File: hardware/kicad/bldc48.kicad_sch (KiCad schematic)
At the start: 0 parts

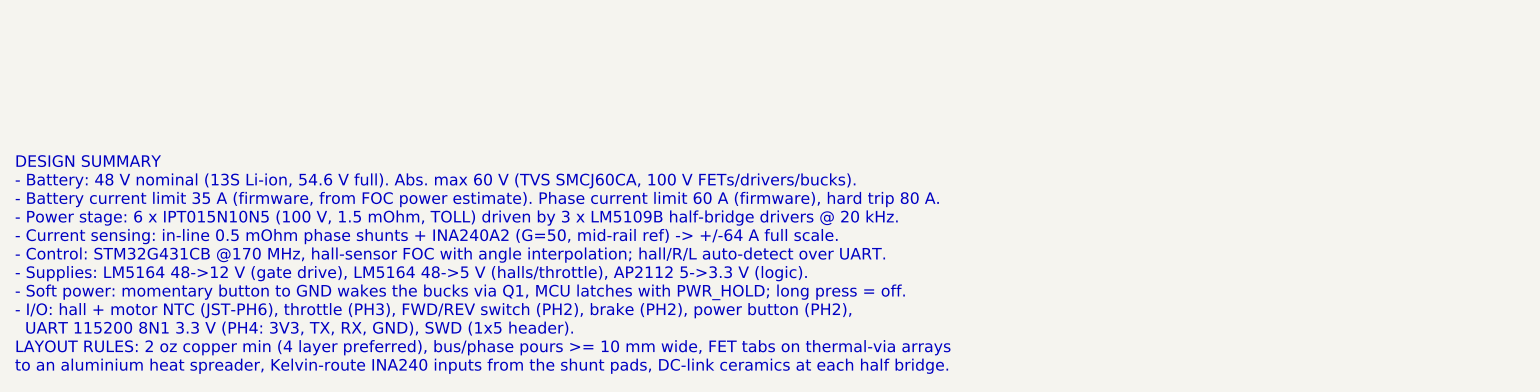
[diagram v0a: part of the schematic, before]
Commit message: Rev B: fix power terminals and design-review findings
Layout (hand-placed power stage):
- BAT+/BAT- and MOTOR A/B/C are now M5 plated bolt terminals at the board
  edges (battery 36 mm apart on the left edge, motors under their shunts),
  replacing 5x10 mm SMD solder pads that sat 7.5 mm apart
- per phase: driver | high FET over low FET (drain tabs up, compact switch
  node) | Kelvin shunt + INA240; DC-link ceramics at the low-side sources
- FET NTC moved next to the middle low-side FET
- rule area keeps tracks off the inner planes under the power stage
- pours sized from real TOLL pad outlines; solid plane connections
- hand route for the one connection Freerouting leaves open; routing
  session saved so the board rebuilds without the autorouter
- KiCad DRC: 0 violations, 0 unconnected, footprints match library

Schematic / firmware:
- INA240A2 -> INA240A1: the 80 A hard trip was above the old +/-66 A ADC
  full scale and could never fire; compile-time assert + sim test added
- 4-terminal Kelvin shunts (BVR 4026) feed the INA240 sense inputs
- gate resistors 10R -> 4R7, bulk caps 6 -> 8

Co-Authored-By: Claude Opus 5.5 <noreply@anthropic.com>
Claude-Session: https://claude.ai/code/session_01KE5bAkgcicsoh5erUtagKE
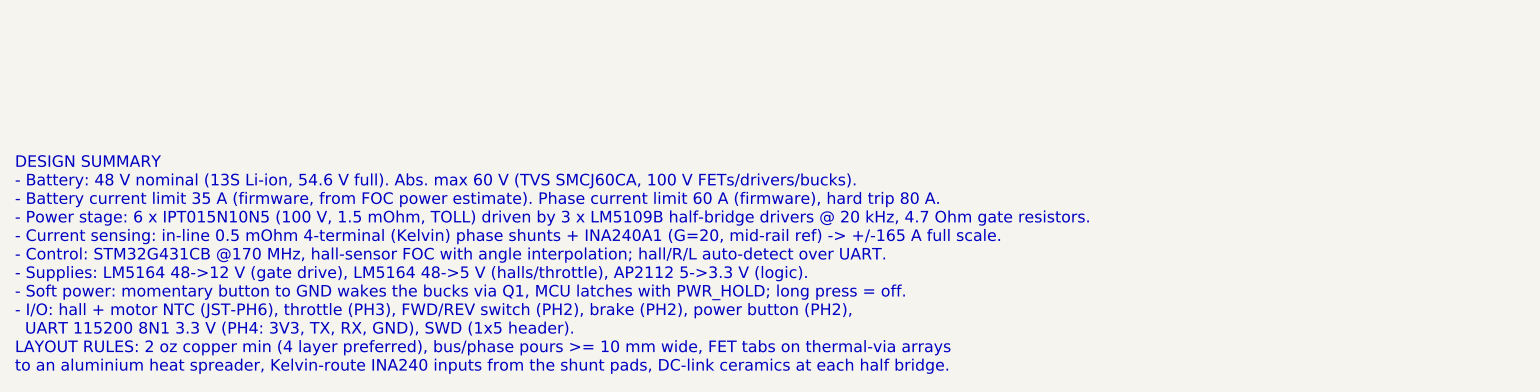
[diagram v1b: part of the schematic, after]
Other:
- note added: "DESIGN SUMMARY - Battery: 48 V nominal (13S Li-ion, 54.6 V full). Abs. max 60 V (TVS SMCJ60CA, 100 V FETs/drivers/bucks). - Battery current limit 35 A (firmware, from FOC power estimate). Phase current limit 60 A (firmware), hard trip 80 A. - Power stage: 6 x IPT015N10N5 (100 V, 1.5 mOhm, TOLL) driven by 3 x LM5109B half-bridge drivers @ 20 kHz, 4.7 Ohm gate resistors. - Current sensing: in-line 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"
- note removed: "DESIGN SUMMARY - Battery: 48 V nominal (13S Li-ion, 54.6 V full). Abs. max 60 V (TVS SMCJ60CA, 100 V FETs/drivers/bucks). - Battery current limit 35 A (firmware, from FOC power estimate). Phase current limit 60 A (firmware), hard trip 80 A. - Power stage: 6 x IPT015N10N5 (100 V, 1.5 mOhm, TOLL) driven by 3 x LM5109B half-bridge drivers @ 20 kHz. - Current sensing: in-line 0.5 mOhm phase shunts + 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"
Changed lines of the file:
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@@
     (rev "A")
     (company "48V 35A hub motor controller")
-    (comment 1 "STM32G431 + LM5109B x3 + IPT015N10N5 x6 + INA240A2 x3")
+    (comment 1 "STM32G431 + LM5109B x3 + IPT015N10N5 x6 + INA240A1 x3")
     (comment 2 "Top level")
   )
@@
     (instances (project "bldc48" (path "/1b798bf4-fe80-550a-af47-9df77e3c6d45" (page "5"))))
   )
-  (text "DESIGN SUMMARY\n- Battery: 48 V nominal (13S Li-ion, 54.6 V full). Abs. max 60 V (TVS SMCJ60CA, 100 V FETs/drivers/bucks).\n- Battery current limit 35 A (firmware, from FOC power estimate). Phase current limit 60 A (firmware), hard trip 80 A.\n- Power stage: 6 x IPT015N10N5 (100 V, 1.5 mOhm, TOLL) driven by 3 x LM5109B half-bridge drivers @ 20 kHz.\n- Current sensing: in-line 0.5 mOhm phase shunts + INA240A2 (G=50, mid-rail ref) -> +/-64 A full scale.\n- Control: STM32G431CB @170 MHz, hall-sensor FOC with angle interpolation; hall/R/L auto-detect over UART.\n- Supplies: LM5164 48->12 V (gate drive), LM5164 48->5 V (halls/throttle), AP2112 5->3.3 V (logic).\n- Soft power: momentary button to GND wakes the bucks via Q1, MCU latches with PWR_HOLD; long press = off.\n- I/O: hall + motor NTC (JST-PH6), throttle (PH3), FWD/REV switch (PH2), brake (PH2), power button (PH2),\n  UART 115200 8N1 3.3 V (PH4: 3V3, TX, RX, GND), SWD (1x5 header).\nLAYOUT RULES: 2 oz copper min (4 layer preferred), bus/phase pours >= 10 mm wide, FET tabs on thermal-via arrays\nto an aluminium heat spreader, Kelvin-route INA240 inputs from the shunt pads, DC-link ceramics at each half bridge." (at 30 185 0) (effects (font (size 1.6 1.6)) (justify left top)))
+  (text "DESIGN SUMMARY\n- Battery: 48 V nominal (13S Li-ion, 54.6 V full). Abs. max 60 V (TVS SMCJ60CA, 100 V FETs/drivers/bucks).\n- Battery current limit 35 A (firmware, from FOC power estimate). Phase current limit 60 A (firmware), hard trip 80 A.\n- Power stage: 6 x IPT015N10N5 (100 V, 1.5 mOhm, TOLL) driven by 3 x LM5109B half-bridge drivers @ 20 kHz, 4.7 Ohm gate resistors.\n- Current sensing: in-line 0.5 mOhm 4-terminal (Kelvin) phase shunts + INA240A1 (G=20, mid-rail ref) -> +/-165 A full scale.\n- Control: STM32G431CB @170 MHz, hall-sensor FOC with angle interpolation; hall/R/L auto-detect over UART.\n- Supplies: LM5164 48->12 V (gate drive), LM5164 48->5 V (halls/throttle), AP2112 5->3.3 V (logic).\n- Soft power: momentary button to GND wakes the bucks via Q1, MCU latches with PWR_HOLD; long press = off.\n- I/O: hall + motor NTC (JST-PH6), throttle (PH3), FWD/REV switch (PH2), brake (PH2), power button (PH2),\n  UART 115200 8N1 3.3 V (PH4: 3V3, TX, RX, GND), SWD (1x5 header).\nLAYOUT RULES: 2 oz copper min (4 layer preferred), bus/phase pours >= 10 mm wide, FET tabs on thermal-via arrays\nto an aluminium heat spreader, Kelvin-route INA240 inputs from the shunt pads, DC-link ceramics at each half bridge." (at 30 185 0) (effects (font (size 1.6 1.6)) (justify left top)))
   (sheet_instances (path "/" (page "1")))
 )

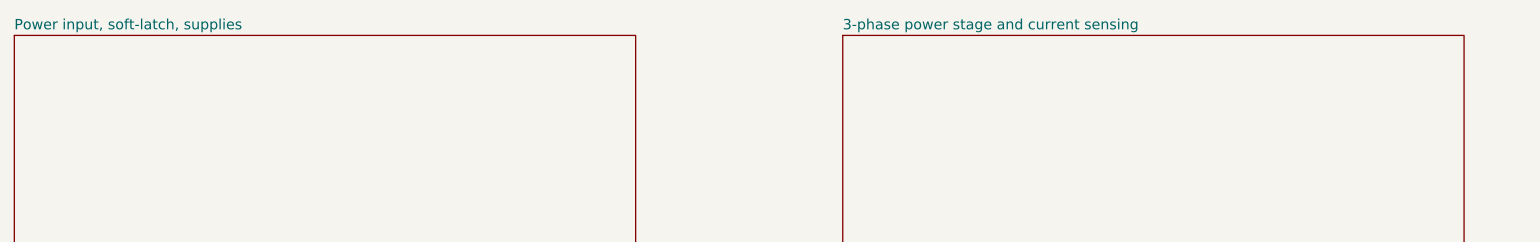
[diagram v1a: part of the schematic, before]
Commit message: Rev F (in progress): DRV8353RS redesign for a 90 x 64.5 mm board
- Circuit: DRV8353RS gate driver + CSAs + 5 V buck replaces 3x LM5109B,
  3x INA240 and both LM5164s; low-side Kelvin shunts; 12 AWG solder-wire
  pads; JST-GH connectors; 3x 1000 uF bulk caps; project symbol/footprint
  library (DRV8353RS symbol + TI RGZ footprint from flatmcu, MIT)
- Firmware: SPI1 driver for the DRV8353 (config + readback + lock, fault
  readout, 'drv' command), ADC sampling at the PWM peak via TIM1 TRGO2,
  high-duty phase rebuilt from the other two, DRIVER fault; sim models the
  low-side shunt blind window and a driver fault - all checks pass
- Placement for the two-sided 3-column layout; router keepouts, pours and
  planes for it (board file stays rev E until routing is done)

Co-Authored-By: Claude Opus 5.5 <noreply@anthropic.com>
Claude-Session: https://claude.ai/code/session_01KE5bAkgcicsoh5erUtagKE
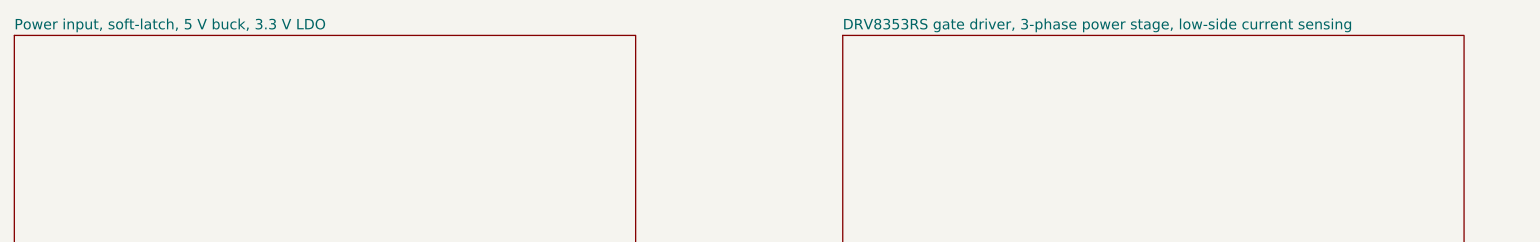
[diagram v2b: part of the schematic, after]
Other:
- sheet 3-phase power stage and current sensing renamed DRV8353RS gate driver, 3-phase power stage, low-side current sensing
- sheet Power input, soft-latch, supplies renamed Power input, soft-latch, 5 V buck, 3.3 V LDO
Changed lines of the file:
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@@
     (rev "A")
     (company "48V 35A hub motor controller")
-    (comment 1 "STM32G431 + LM5109B x3 + IPT015N10N5 x6 + INA240A1 x3")
+    (comment 1 "STM32G431 + DRV8353RS + IPT015N10N5 x6, low-side Kelvin shunts")
     (comment 2 "Top level")
   )
   (sheet (at 30 50) (size 90 35) (fields_autoplaced)
     (stroke (width 0.1524) (type solid)) (fill (color 0 0 0 0.0000))
-    (property "Sheetname" "Power input, soft-latch, supplies" (at 30 49.3 0) (effects (font (size 1.5 1.5)) (justify left bottom)))
+    (property "Sheetname" "Power input, soft-latch, 5 V buck, 3.3 V LDO" (at 30 49.3 0) (effects (font (size 1.5 1.5)) (justify left bottom)))
     (property "Sheetfile" "power.kicad_sch" (at 30 85.6 0) (effects (font (size 1.27 1.27)) (justify left top)))
     (instances (project "bldc48" (path "/1b798bf4-fe80-550a-af47-9df77e3c6d45" (page "2"))))
@@
   (sheet (at 150 50) (size 90 35) (fields_autoplaced)
     (stroke (width 0.1524) (type solid)) (fill (color 0 0 0 0.0000))
-    (property "Sheetname" "3-phase power stage and current sensing" (at 150 49.3 0) (effects (font (size 1.5 1.5)) (justify left bottom)))
+    (property "Sheetname" "DRV8353RS gate driver, 3-phase power stage, low-side current sensing" (at 150 49.3 0) (effects (font (size 1.5 1.5)) (justify left bottom)))
     (property "Sheetfile" "bridge.kicad_sch" (at 150 85.6 0) (effects (font (size 1.27 1.27)) (justify left top)))
     (instances (project "bldc48" (path "/1b798bf4-fe80-550a-af47-9df77e3c6d45" (page "3"))))
